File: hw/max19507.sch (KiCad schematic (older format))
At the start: 33 parts, among them J6 BNC, J8 BNC, U8 THS4522, U9 MAX19507

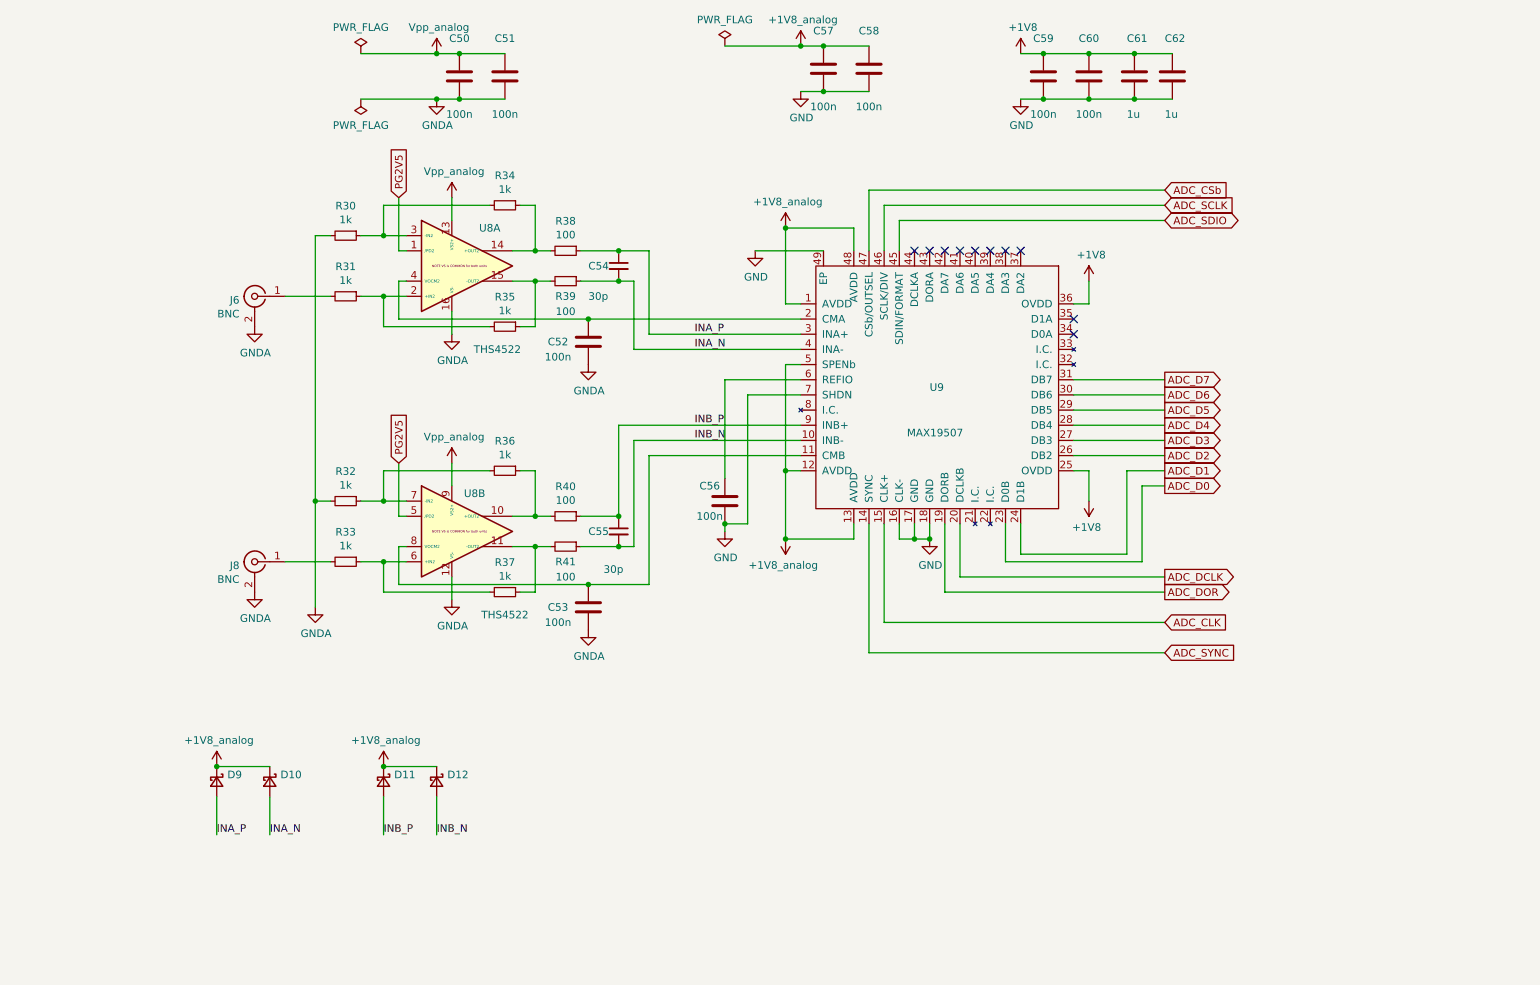
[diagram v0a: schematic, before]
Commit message: Started to work on analog front-end; ADC connected to fpga
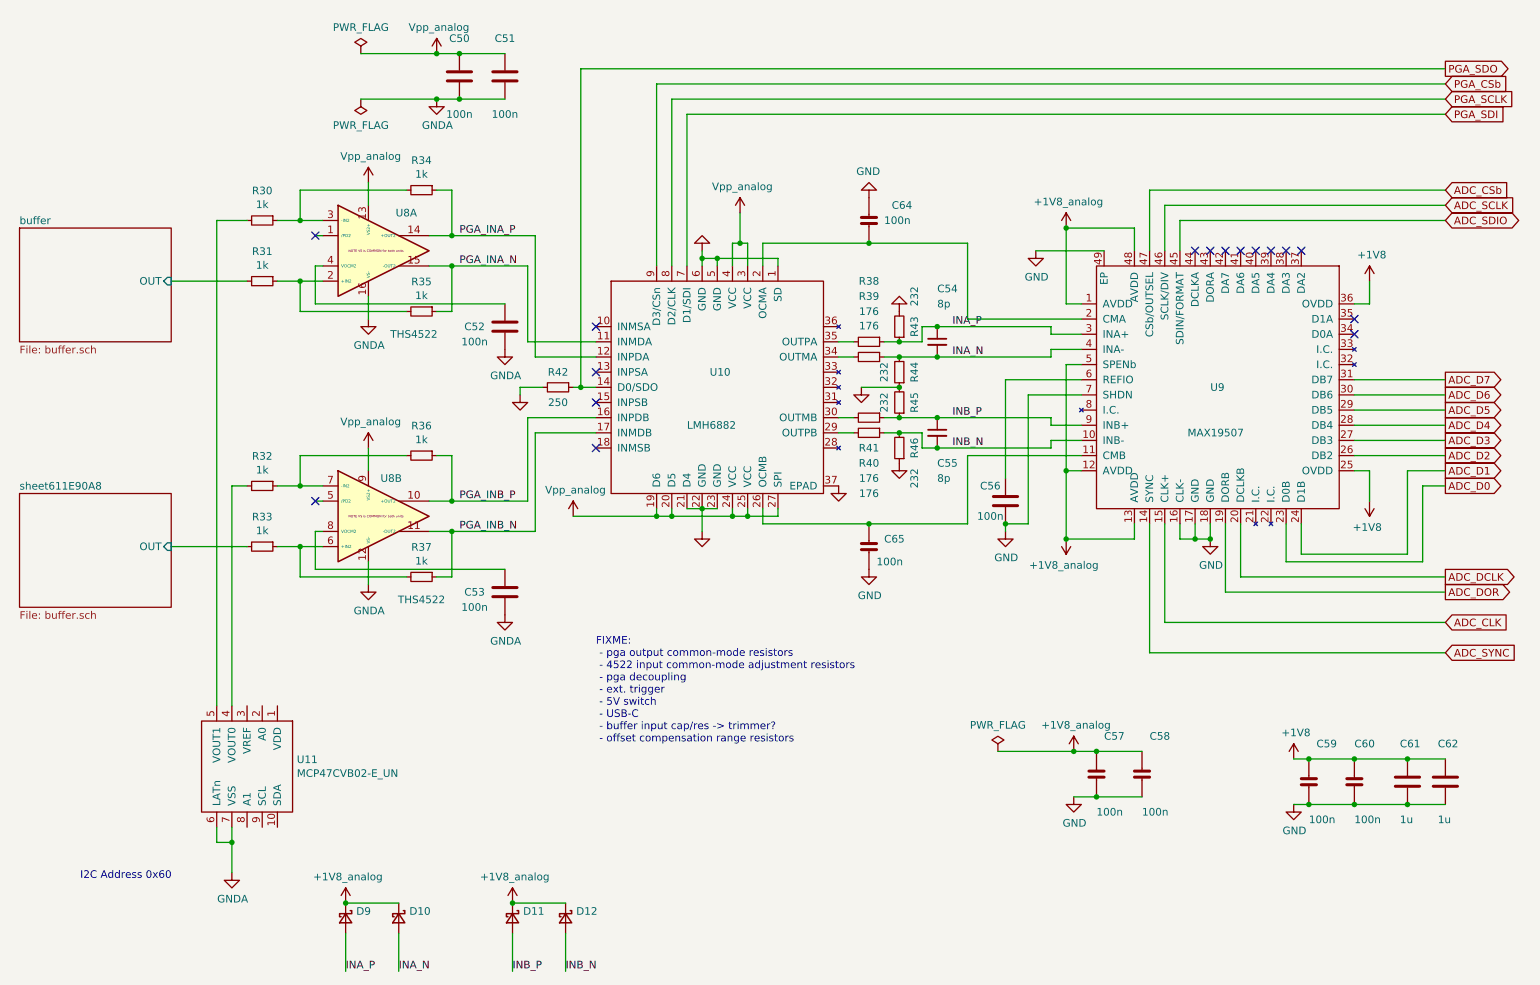
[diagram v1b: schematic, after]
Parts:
- removed C57, C58, C59, C60: 100n, Capacitor_SMD:C_0603_1608Metric, symbol fmc:100nF_603
- removed J6, J8: BNC, proj_footprints:BNC_Molex_0731713150, symbol Connector:Conn_Coaxial
- added C57, C58, C59, C60, C64, C65: 100n, Capacitor_SMD:C_0402_1005Metric, symbol fmc:100nF_402
- added R42: 250, Resistor_SMD:R_0603_1608Metric, symbol Device:R_Small
- added R43, R44, R45, R46: 232, Resistor_SMD:R_0603_1608Metric, symbol Device:R_Small
- added U10: LMH6882, Package_DFN_QFN:Texas_S-PVQFN-N36_EP4.4x4.4mm_ThermalVias, symbol fmc:LMH6882
- added U11: MCP47CVB02-E_UN, Package_SO:MSOP-10_3x3mm_P0.5mm, symbol fmc:MCP47CVB02-E_UN
- C54, C55: value 30p -> 8p
- R38, R39, R40, R41: value 100 -> 176
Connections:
- net +1V8: now also C59.1, C60.1
- net +1V8_analog: now also C57.1, C58.1
- net GND: now also C57.2, C58.2, C59.2, C60.2, C64.1, C65.2, R42.2, R43.2, R44.1, R45.2, R46.1, U10.1 (SD), U10.21 (D4), U10.22 (GND), U10.23 (GND), U10.37 (EPAD), U10.5 (GND), U10.6 (GND)
- net GNDA: now also U11.6 (LATn), U11.7 (VSS); no longer R30.2, R32.2
- net INA_N: now also R44.2
- net INA_P: now also R43.1
- net INB_N: now also R46.2
- net INB_P: now also R45.1
- net Vpp_analog: now also U10.19 (D6), U10.20 (D5), U10.24 (VCC), U10.25 (VCC), U10.27 (SPI), U10.3 (VCC), U10.4 (VCC)
- net buffer/OUT: now reaches R31.2
- net sheet611E90A8/OUT: now reaches R33.2
- net PGA_INA_P: now reaches R34.1, U8.14 (+OUT2)
- net PGA_INA_P: now also U10.12 (INPDA); no longer R38.2
- net PGA_INA_N: now reaches R35.1, U8.15 (-OUT2)
- net PGA_INA_N: now also U10.11 (INMDA); no longer R39.2
- net at C52.2, U8.4 (VOCM2): no longer U9.2 (CMA)
- net PGA_INB_P: now reaches R36.1, U8.10 (+OUT2)
- net PGA_INB_P: now also U10.16 (INPDB); no longer R40.2
- net PGA_INB_N: now reaches R37.1, U8.11 (-OUT2)
- net PGA_INB_N: now also U10.17 (INMDB); no longer R41.2
- net at C53.2, U8.8 (VOCM2): no longer U9.11 (CMB)
- net PG2V5: no longer names the net of U8.1 (/PD2)
- net PG2V5: no longer U8.5 (/PD2)
- new net: C64.2, U10.2 (OCMA), U9.2 (CMA)
- new net: C65.1, U10.26 (OCMB), U9.11 (CMB)
- new net: R41.2, U10.29 (OUTPB)
- new net: R40.2, U10.30 (OUTMB)
- new net: R39.2, U10.34 (OUTMA)
- new net: R38.2, U10.35 (OUTPA)
- new net: R32.2, U11.4 (VOUT0)
- new net: R30.2, U11.5 (VOUT1)
- new net PGA_CSb: U10.9 (D3/CSn)
- new net PGA_SCLK: U10.8 (D2/CLK)
- new net PGA_SDI: U10.7 (D1/SDI)
- new net PGA_SDO: R42.1, U10.14 (D0/SDO)
- no-connect marks 10 -> 16
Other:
- note added: "FIXME:\n - pga output common-mode resistors\n - 4522 input common-mode adjustment resistors\n - pga decoupling\n - ext. trigger\n - 5V switch\n - USB-C\n - buffer input cap/res -> trimmer?\n - offset compensation range resistors"
- note added: "I2C Address 0x60"
- moved on the sheet: C52, C53, C54, C55, C56, C61, C62, D10, D11, D12, D9, R30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

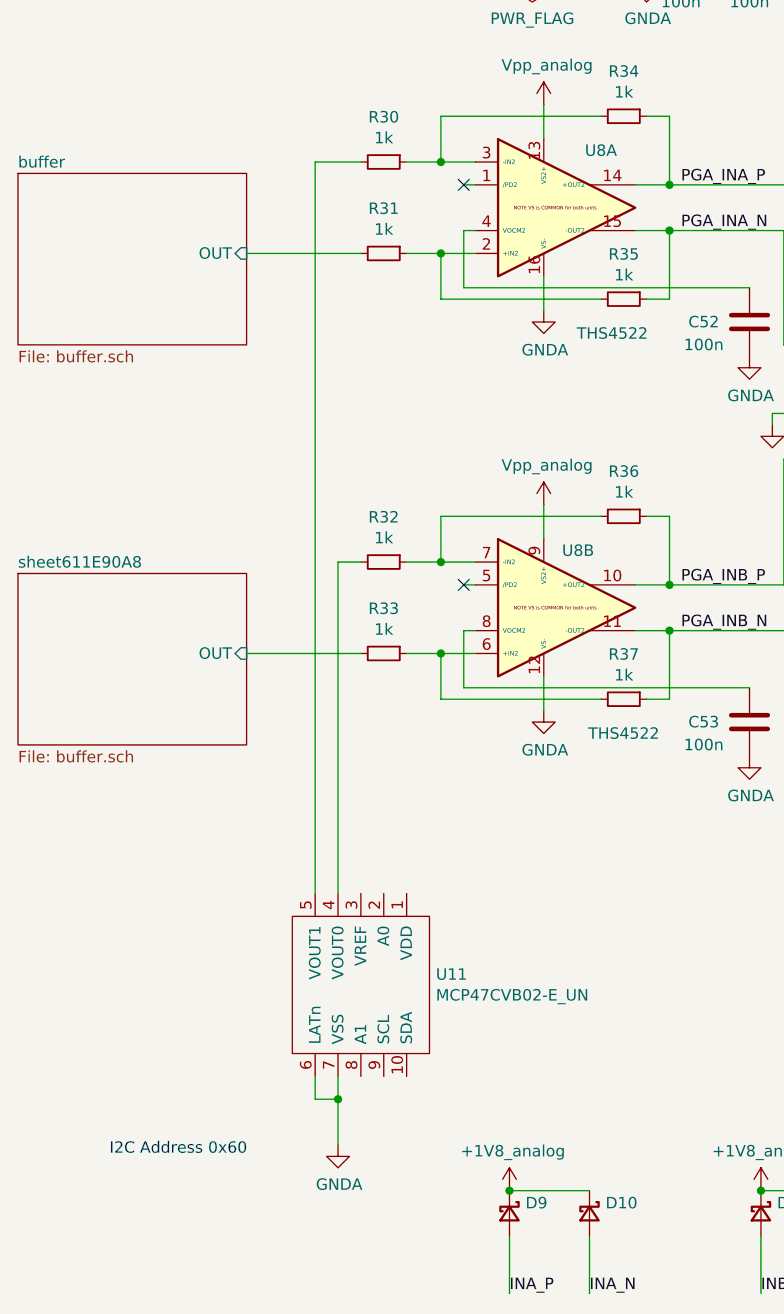
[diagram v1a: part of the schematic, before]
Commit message: added buffer amps for offset dac
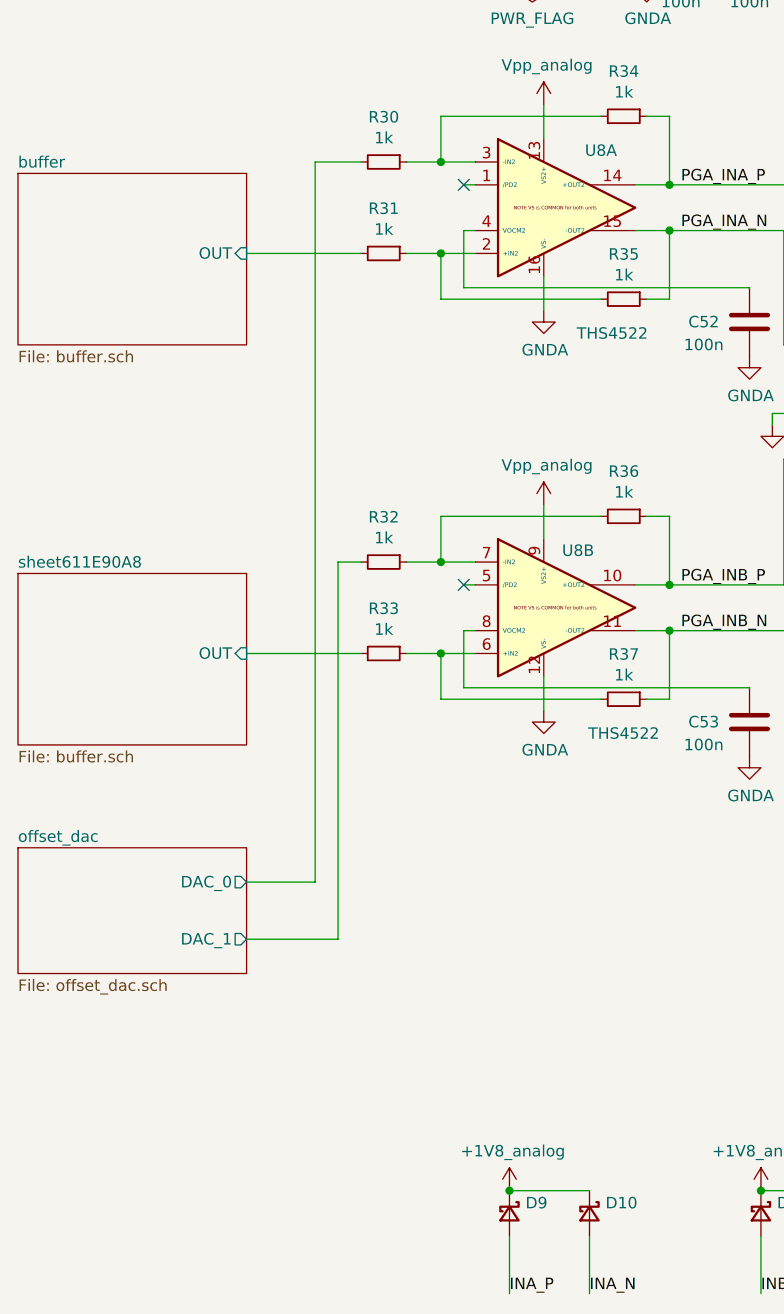
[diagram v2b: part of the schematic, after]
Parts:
- removed U11: MCP47CVB02-E_UN, Package_SO:MSOP-10_3x3mm_P0.5mm, symbol fmc:MCP47CVB02-E_UN
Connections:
- net offset_dac/DAC_1: now reaches R32.2
- net offset_dac/DAC_0: now reaches R30.2
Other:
- note removed: "I2C Address 0x60"
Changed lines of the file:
@@
 $Descr A4 11693 8268
 encoding utf-8
-Sheet 5 7
+Sheet 5 8
 Title ""
 Date ""
@@
 Text Notes 4750 5750 0    50   ~ 0
 FIXME:\n - pga output common-mode resistors\n - 4522 input common-mode adjustment resistors\n - pga decoupling\n - ext. trigger\n - 5V switch\n - USB-C\n - buffer input cap/res -> trimmer?\n - offset compensation range resistors
-$Comp
-L fmc:MCP47CVB02-E_UN U11
-U 1 1 612145E1
-P 2450 5900
-F 0 "U11" V 2404 6228 50  0000 L CNN
-F 1 "MCP47CVB02-E_UN" V 2495 6228 50  0000 L CNN
-F 2 "Package_SO:MSOP-10_3x3mm_P0.5mm" H 2450 5850 50  0001 C CNN
-F 3 "" H 2450 5850 50  0001 C CNN
-F 4 "MCP47CVB02-E_UN" H 2450 5900 50  0001 C CNN "Part"
-F 5 "MicroChip" H 2450 5900 50  0001 C CNN "Manufacturer"
-	1    2450 5900
-	0    1    1    0
-$EndComp
-$Comp
-L power:GNDA #PWR?
-U 1 1 612301C7
-P 2350 6600
-F 0 "#PWR?" H 2350 6350 50  0001 C CNN
-F 1 "GNDA" H 2355 6427 50  0000 C CNN
-F 2 "" H 2350 6600 50  0001 C CNN
-F 3 "" H 2350 6600 50  0001 C CNN
-	1    2350 6600
-	1    0    0    -1
-$EndComp
-Wire Wire Line
-	2350 6300 2350 6400
-Wire Wire Line
-	2350 4050 2350 5500
-Wire Wire Line
-	2250 2300 2250 5500
 Wire Wire Line
 	2250 2300 2450 2300
-Wire Wire Line
-	2250 6300 2250 6400
-Wire Wire Line
-	2250 6400 2350 6400
-Connection ~ 2350 6400
-Wire Wire Line
-	2350 6400 2350 6600
-Text Notes 1350 6650 0    50   ~ 0
-I2C Address 0x60
+$Sheet
+S 950  5300 1000 550
+U 60C14D80
+F0 "offset_dac" 50
+F1 "offset_dac.sch" 50
+F2 "DAC_0" O R 1950 5450 50
+F3 "DAC_1" O R 1950 5700 50
+$EndSheet
+Wire Wire Line
+	2250 2300 2250 5450
+Wire Wire Line
+	2250 5450 1950 5450
+Wire Wire Line
+	2350 4050 2350 5700
+Wire Wire Line
+	2350 5700 1950 5700
 $EndSCHEMATC

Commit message: more work (don't recall details :-()
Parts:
- added C57, C83, C84, C91, C94, C95: 10n, Capacitor_SMD:C_0402_1005Metric, symbol fmc:100nF_402
- added C92, C93: 15p, Capacitor_SMD:C_0603_1608Metric, symbol Device:C_Small
- added C96, C97: 1u, Capacitor_SMD:C_0805_2012Metric, symbol fmc:1uF_805
- added R57, R59: 232, Resistor_SMD:R_0603_1608Metric, symbol Device:R_Small
- C54, C55: value 8p -> 15p
- renumbered C57 to C49
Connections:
- net +1V8_analog: no longer U9.5 (SPENb)
- net GND: now also C54.2, C55.1, U9.5 (SPENb), C92.1, C93.2; no longer C49.2, C58.2, C64.1, C65.2, U10.1 (SD), U10.21 (D4), U10.22 (GND), U10.23 (GND), U10.37 (EPAD), U10.5 (GND), U10.6 (GND)
- net GNDA: now also C49.2, C58.2, C64.1, C65.2, U10.1 (SD), U10.21 (D4), U10.22 (GND), U10.23 (GND), U10.37 (EPAD), U10.5 (GND), U10.6 (GND), C57.2, C83.2, C84.2, C91.2, C94.2, C95.2, C96.2, C97.2
- net INA_N: now also C54.1, R57.1; no longer C54.2
- net INA_P: now also C92.2, R57.2; no longer C54.1
- net INB_N: now also C93.1, R59.1; no longer C55.2
- net INB_P: now also C55.2, R59.2; no longer C55.1
- net PGA_INB_N: now also U10.16 (INPDB); no longer U10.17 (INMDB)
- net PGA_INB_P: now also U10.17 (INMDB); no longer U10.16 (INPDB)
- net Vpp_analog: now also C57.1, C83.1, C84.1, C91.1, C94.1, C95.1, C96.1, C97.1
- net offset_dac/DAC_1: now also R33.2; no longer R32.2
- net sheet611E90A8/OUT: now also R32.2; no longer R33.2
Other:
- note added: "FIXME:\n - ext. trigger\n - 5V switch\n- keepouts under L (power), opamps"
- note removed: "FIXME:\n - pga output common-mode resistors\n - 4522 input common-mode adjustment resistors\n - pga decoupling\n - ext. trigger\n - 5V switch\n - USB-C\n - buffer input cap/res -> trimmer?\n - offset compensation range resistors"
- moved on the sheet: C54, C55
